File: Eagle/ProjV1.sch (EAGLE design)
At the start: 24 parts, among them IC1 CD4007UBM, IC2 CD4007UBM, IC3 CD4007UBM, SW1 EC12E_SW, U1 MIC5504-3.3YM5-T5, U2 MCP2200-I/SS, U3 ATMEGA328PB-AU, Y1 16MHz

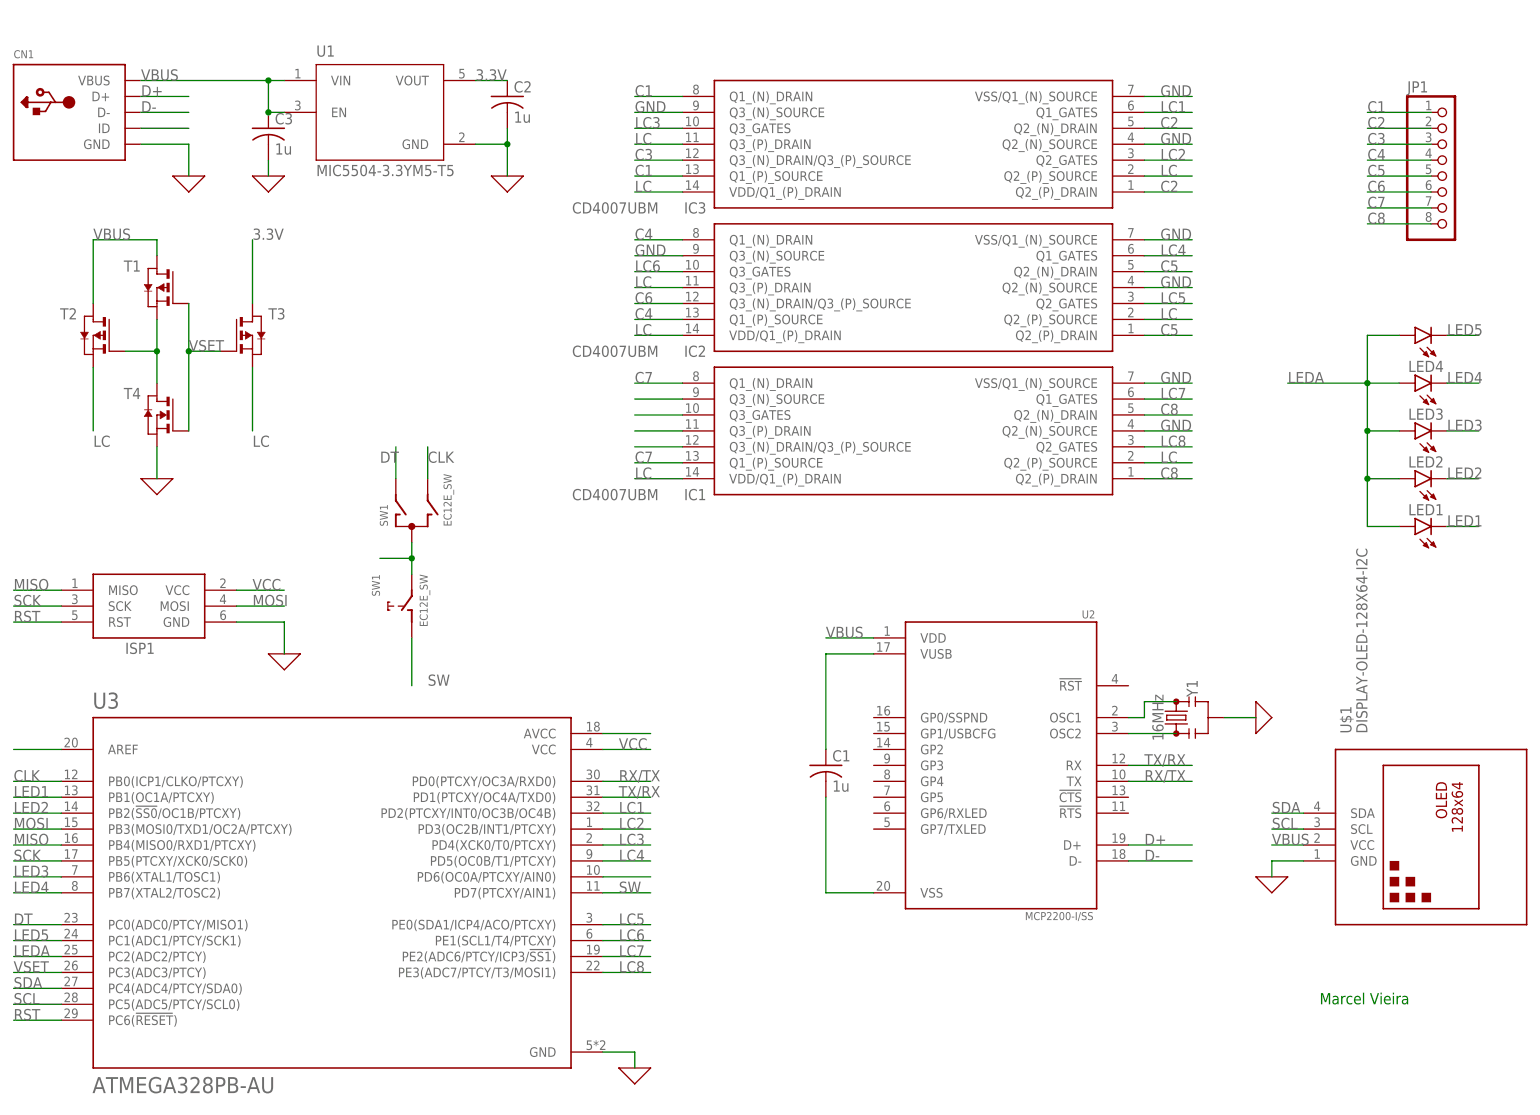
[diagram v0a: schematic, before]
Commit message: Schematic Changes
Added votage and ground flags and switched to running board at 3.3V
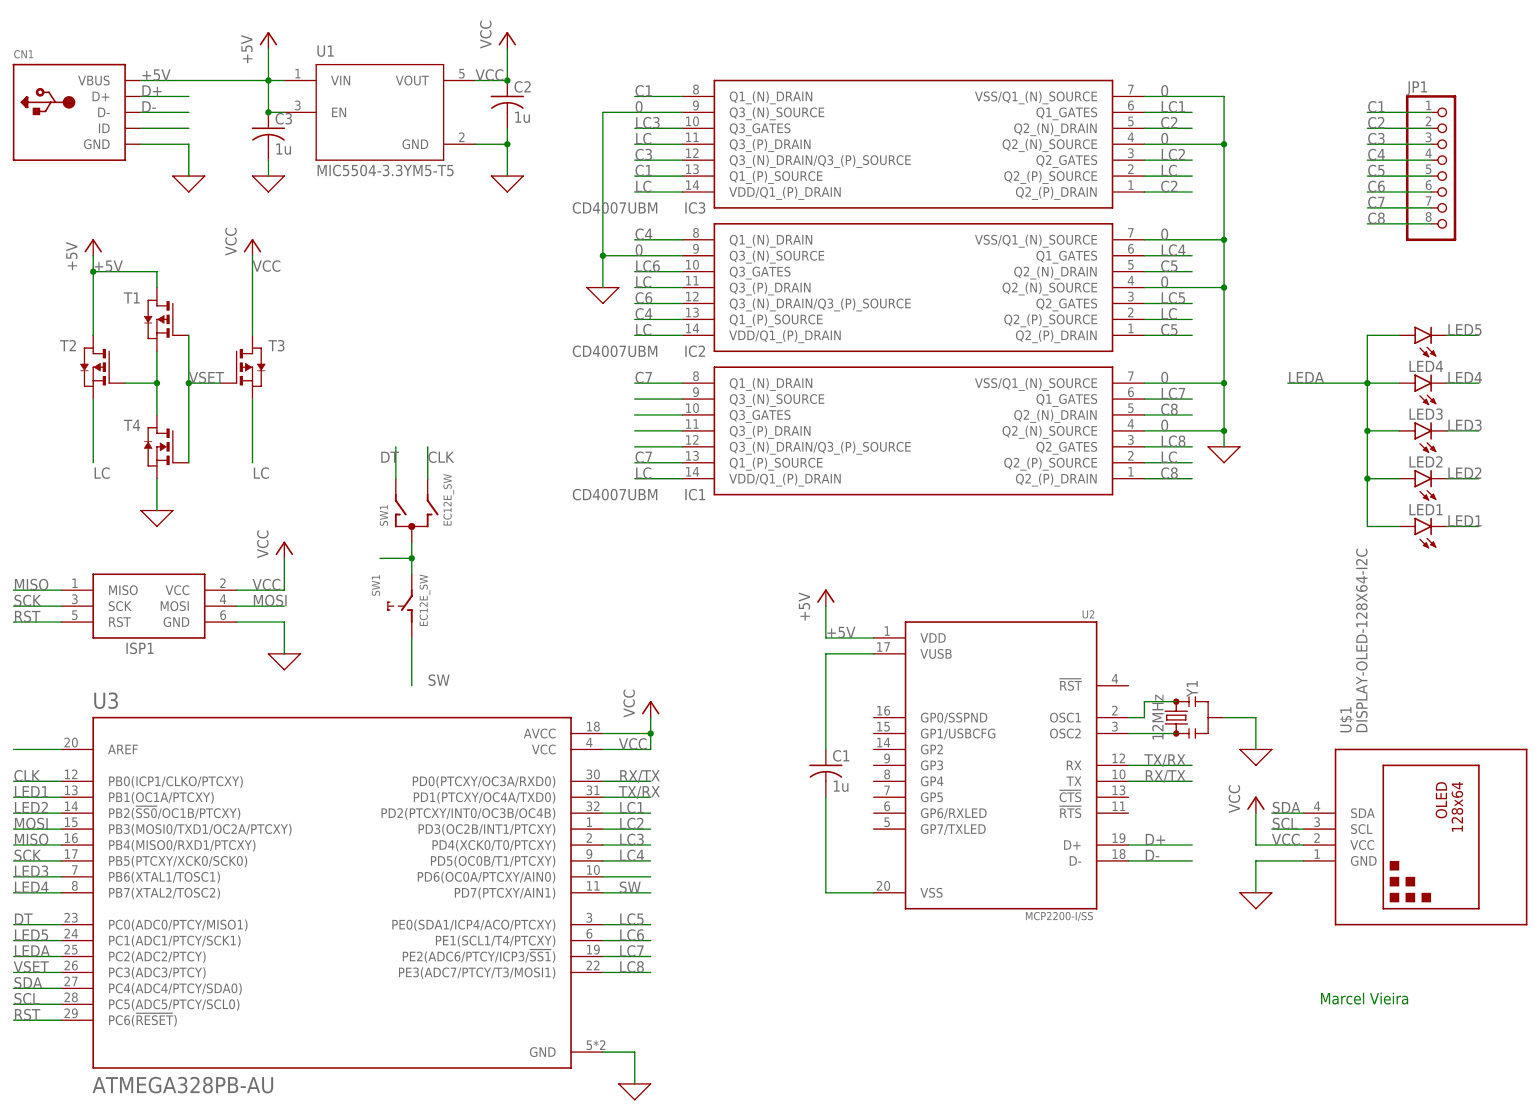
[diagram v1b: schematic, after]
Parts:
- Y1: value 16MHz -> 12MHz
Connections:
- removed net 3.3V: C2.1, T3.D, U1.VOUT
- removed net GND: IC1.Q2_(N)_SOURCE, IC1.VSS/Q1_(N)_SOURCE, IC2.Q2_(N)_SOURCE, IC2.Q3_(N)_SOURCE, IC2.VSS/Q1_(N)_SOURCE, IC3.Q2_(N)_SOURCE, IC3.Q3_(N)_SOURCE, IC3.VSS/Q1_(N)_SOURCE
- removed net N$31: U3.AVCC
- removed net VBUS: C3.1, CN1.VBUS, T1.D, T2.D, U$1.VCC, U1.EN, U1.VIN, U2.VDD
- new net +5V: C3.1, CN1.VBUS, T1.D, T2.D, U1.EN, U1.VIN, U2.VDD
- net 0: now also IC1.Q2_(N)_SOURCE, IC1.VSS/Q1_(N)_SOURCE, IC2.Q2_(N)_SOURCE, IC2.Q3_(N)_SOURCE, IC2.VSS/Q1_(N)_SOURCE, IC3.Q2_(N)_SOURCE, IC3.Q3_(N)_SOURCE, IC3.VSS/Q1_(N)_SOURCE
- net VCC: now also C2.1, T3.D, U$1.VCC, U1.VOUT, U3.AVCC
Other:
- moved on the sheet: T1, T2, T3, T4
